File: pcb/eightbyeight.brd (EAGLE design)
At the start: 60 x 60 mm, 163 parts, among them J1 USB_MICROSMT+THRUHULE, J2 BATTERY, Q1 16MHz, SW1 SWITCH_SPDT, SW2 BRIGHTNESS, U1 MK20DN64VFM5, U10 FDG6316P, U11 FDG6316P, U12 FDG6316P, U2 ICN2026, U3 74138, U4 ICN2026, U5 MIC5219 3.3V, U6 ESP_WROOM_02, U7 MP3401A, U8 MMA8653FC, U9 FDG6316P

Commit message: Add HRC art
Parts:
- R28: value DNP -> 10k
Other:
- outline, holes or cut-outs redrawn
- board text added: "EightByEight RevF 2016-07"
- board text added: "Silk layers: 200: 2 sigma front (LED side) 201: 2 sigma back (component side) 203: HRC front (LED side) 204: Blinkinlabs front (LED side)"
- board text removed: "EightByEight RevE 2016-07"

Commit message: Production silk and component values
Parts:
- R1: value 1.6k 1% -> 1k 1%
- R9: value 2k 1% -> 1k 1%
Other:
- board text added: "Silk layers: 200: 2 sigma bottom (LED side) 201: 2 sigma top (component side) 203: HRC back (LED side) 204: Labels top (component side) 206: Blinkinlabs top (component side)"
- board text removed: "16"
- board text removed: "3.3V"
- board text removed: "5"
- board text removed: "Blinkinlabs, LLC"
- board text removed: "Charge"
- board text removed: "EightByEight RevF 2016-07"
- board text removed: "GND"
- board text removed: "Off"
- board text removed: "On"
- board text removed: "Power"
- board text removed: "Silk layers: 200: 2 sigma front (LED side) 201: 2 sigma back (component side) 203: HRC front (LED side) 204: Blinkinlabs front (LED side)"

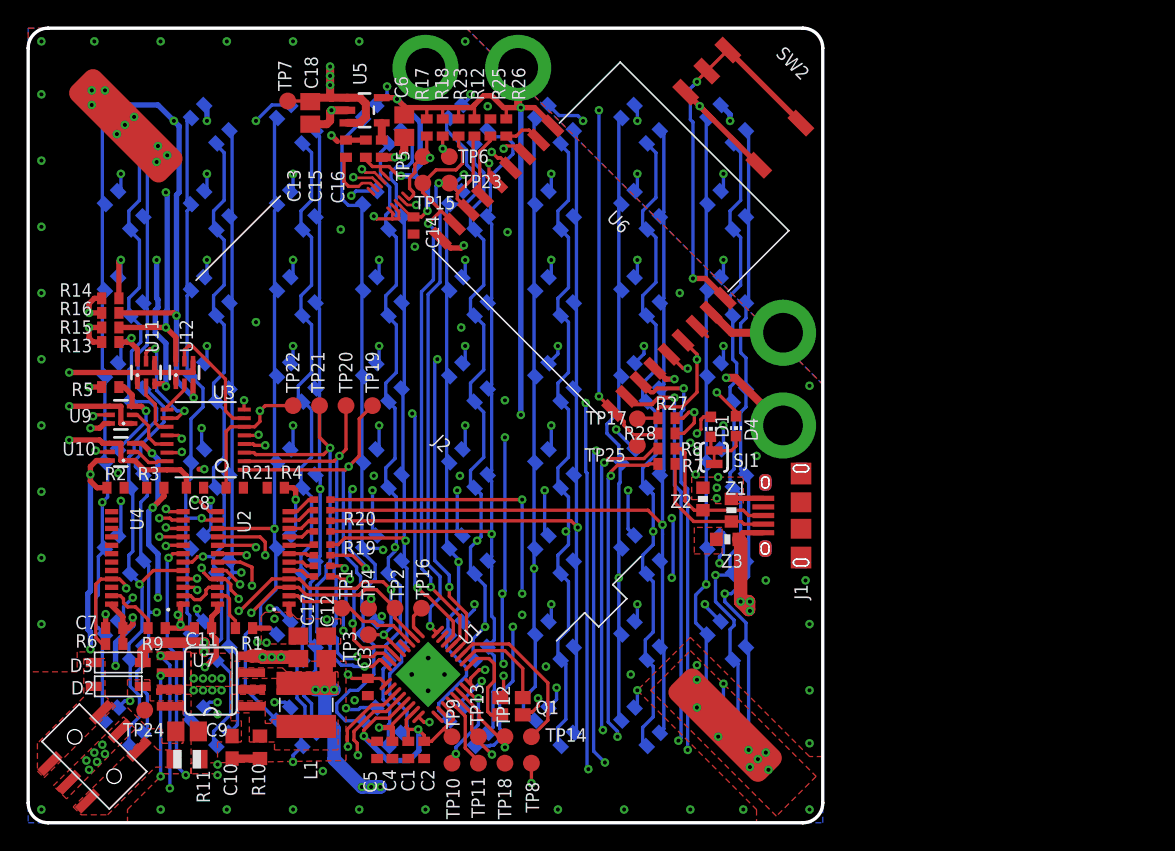
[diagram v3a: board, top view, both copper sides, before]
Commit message: Add battery protection circuit
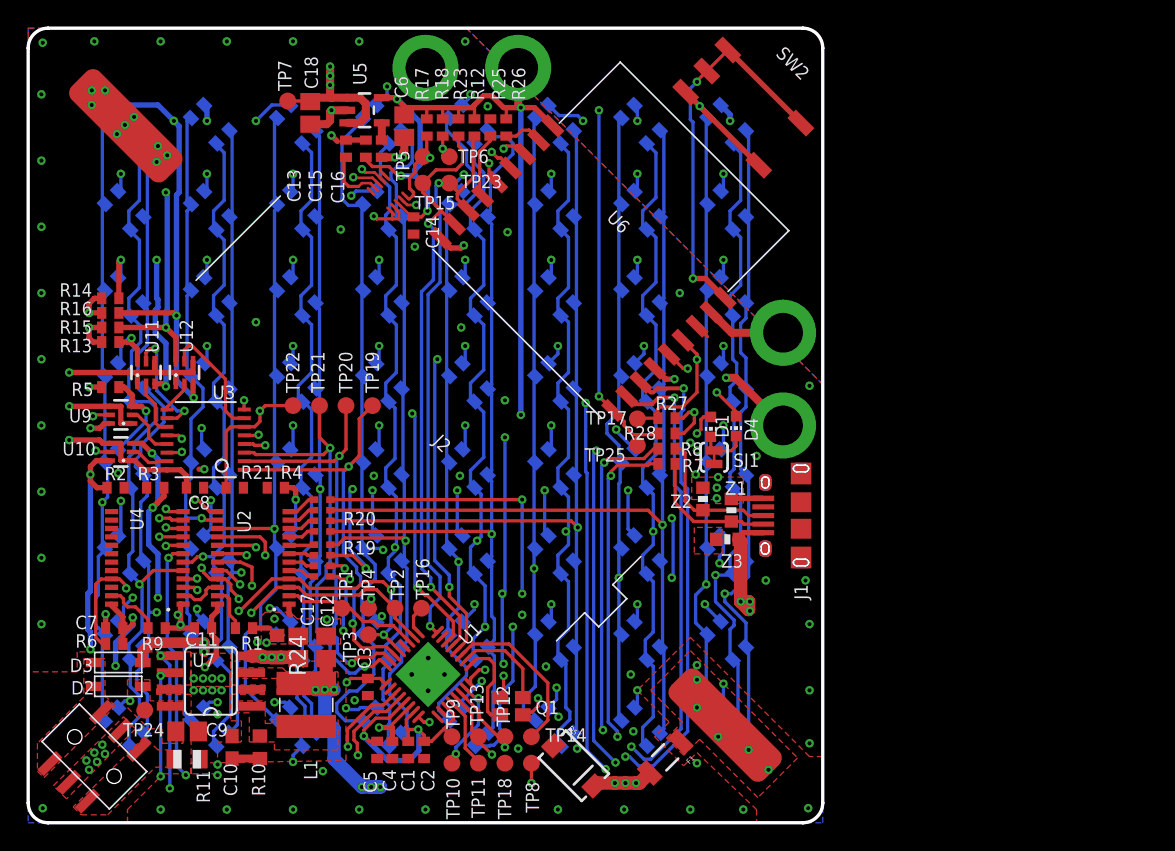
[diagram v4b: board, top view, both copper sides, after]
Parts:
- added D5: 1N5822, SparkFun-DiscreteSemi:SMA-DIODE
- added F1: PTCSMD-W, SparkFun-PowerIC:PTC-1206-WIDE
- added R24: 510, adafruit:R0603
- D2, D3: value RB161M-20 -> 1N5819
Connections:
- new net VBAT_FUSED: C12.1, D5.C, F1.2, L1.P$1, TP8.TP, U7.3
- net GND: now also D5.A, R24.1
- net USB_5V: now also R24.2
- net VBAT: now also F1.1; no longer C12.1, L1.P$1, TP8.TP, U7.3
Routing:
- net VBAT: track 46.6 -> 0.00 mm, vias 16 -> 6
- net VBAT_FUSED: track 0.00 -> 40.5 mm, vias 0 -> 10
- net DISCHARGE: track 84.0 -> 85.8 mm
- net CHARGE: track 77.2 -> 78.3 mm
- net ARM_TX: track 49.4 -> 50.1 mm
- net GND: vias 102 -> 107
- added copper zone on layer 1, net VBAT_FUSED

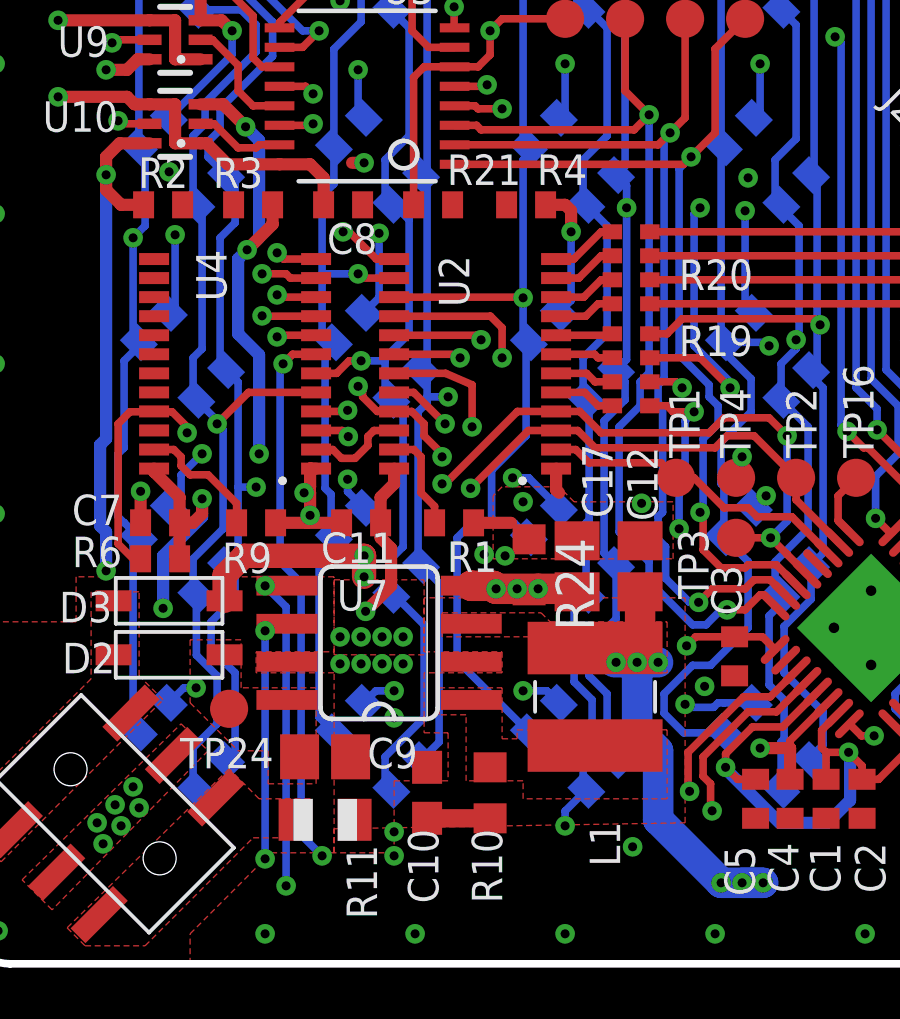
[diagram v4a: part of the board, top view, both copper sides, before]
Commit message: Add seperate bleed resistor to 5V input
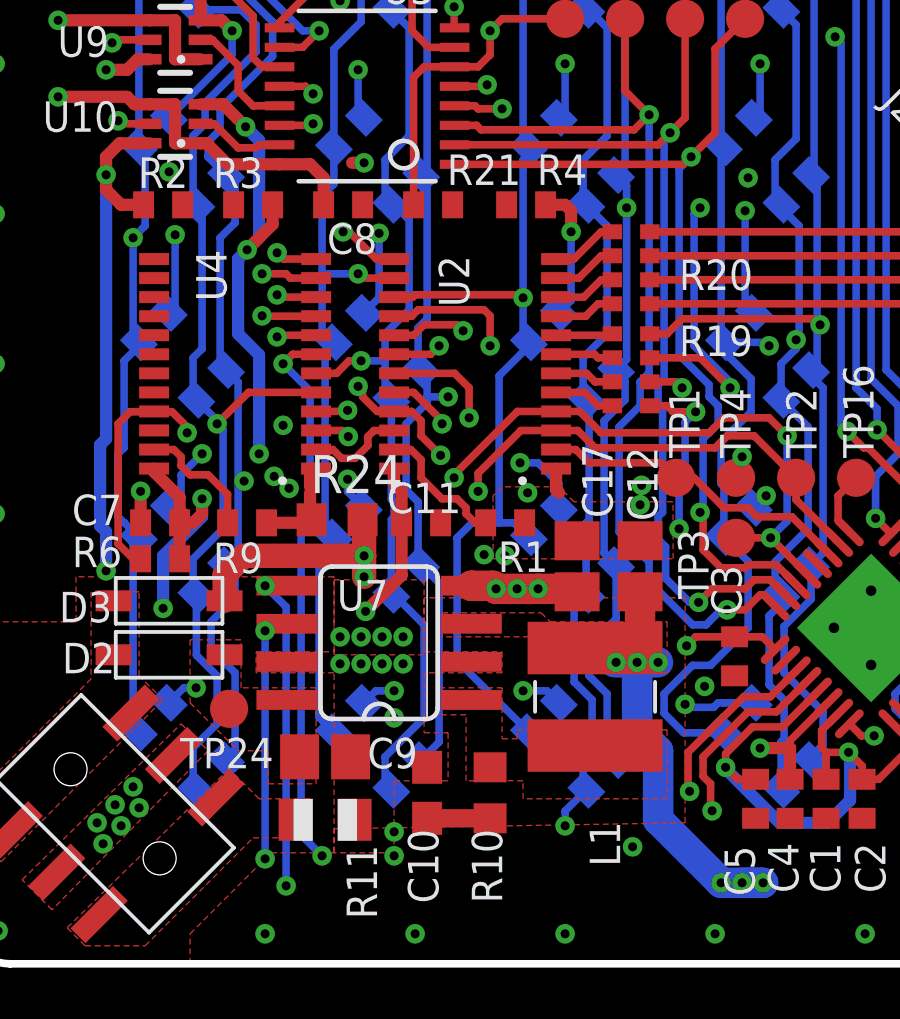
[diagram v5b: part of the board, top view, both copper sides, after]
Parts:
- moved R24 6.57 mm to (12.4, 14.8), turned to 0 degrees
- moved C11 2.00 mm to (15.2, 14.7), turned to 0 degrees
- moved R1 1.70 mm to (18.0, 14.7)
- moved R9 0.30 mm to (9.40, 14.7)
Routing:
- net GND: track 73.3 -> 70.7 mm, vias 107 -> 109
- net 1ROW1: track 73.1 -> 74.3 mm
- net USB_5V: track 65.4 -> 66.7 mm
- net N$18: track 3.39 -> 4.53 mm

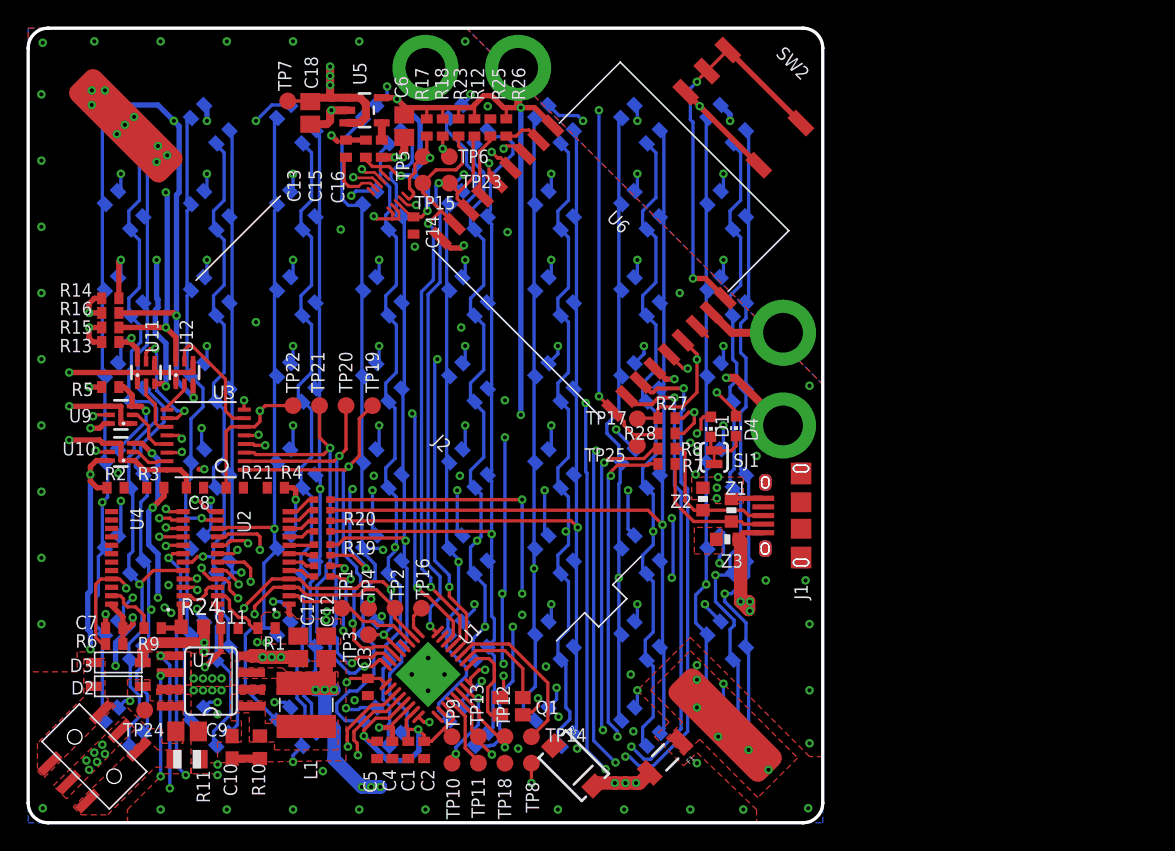
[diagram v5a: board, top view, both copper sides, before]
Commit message: Replace 0402 components, add RevH notes
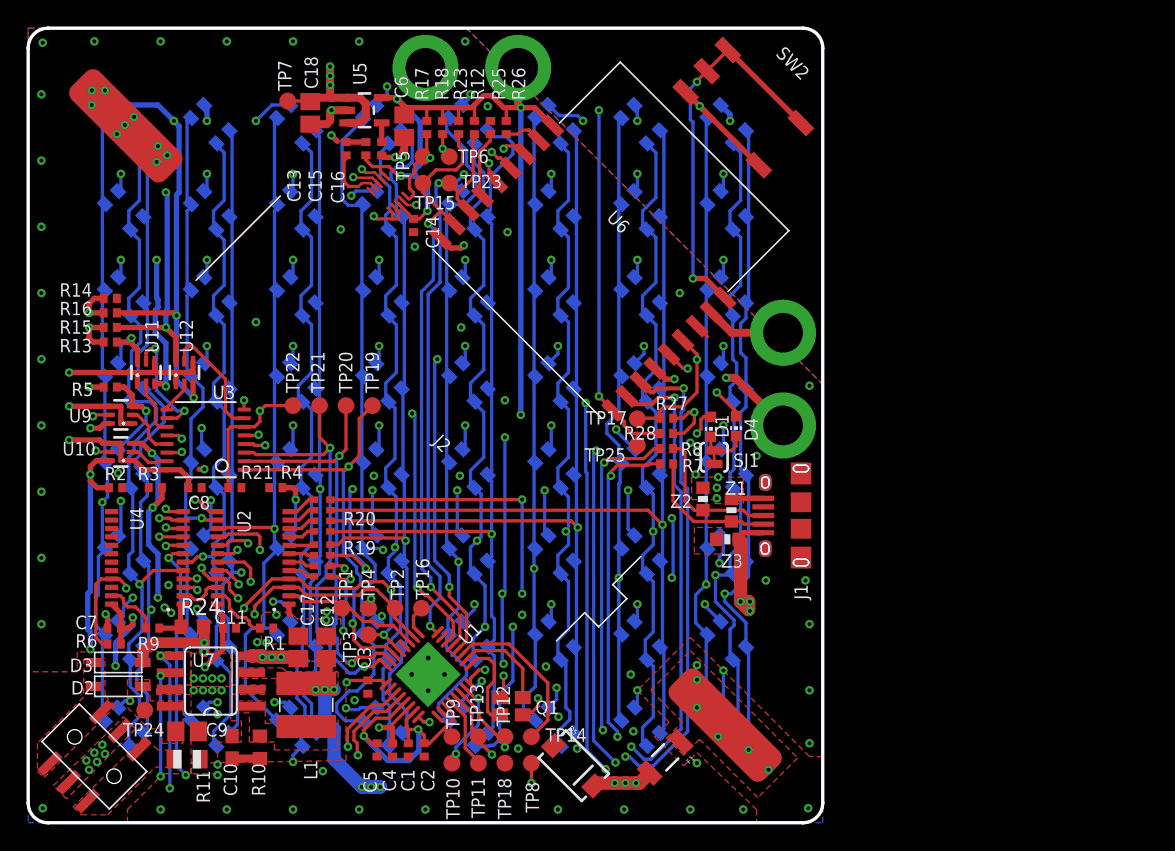
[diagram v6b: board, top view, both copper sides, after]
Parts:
- C1, C11, C13, C14, C15, C16, C2, C3, C4, C5, C7, C8: device adafruit:C0402 -> DevicesToMerge:CAP_0402
- J2: value BATTERY -> BATTERYAA_SMD
- LED_1, LED_10, LED_11, LED_12, LED_13, LED_14, LED_15, LED_16, LED_17, LED_18, LED_19, LED_2, LED_20, LED_21, LED_22, LED_23, LED_24, LED_25, LED_26, LED_27, LED_28, LED_29, LED_3, LED_30, LED_31, LED_32, LED_33, LED_34, LED_35, LED_36, LED_37, LED_38, LED_39, LED_4, LED_40, LED_41, LED_42, LED_43, LED_44, LED_45, LED_46, LED_47, LED_48, LED_49, LED_5, LED_50, LED_51, LED_52, LED_53, LED_54, LED_55, LED_56, LED_57, LED_58, LED_59, LED_6, LED_60, LED_61, LED_62, LED_63, LED_64, LED_7, LED_8, LED_9: value LED_RGB_CA -> LED_RGB_CA3528
- R1, R12, R13, R14, R15, R16, R17, R18, R2, R21, R23, R25, R26, R27, R28, R3, R4, R5, R6, R7, R8, R9: device adafruit:R0402 -> DevicesToMerge:RESISTOR_0402
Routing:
- net 1ROW5: track 70.5 -> 67.5 mm
- net 1ROW0: track 85.7 -> 87.2 mm
- net +3V3: track 81.2 -> 82.5 mm
- net ARM_3V3: track 64.0 -> 65.0 mm
- net GND: track 70.7 -> 71.4 mm
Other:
- board text added: "EightByEight Blinky 2017-02-11 RevH"

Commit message: Use copper fills for 5v, battery traces
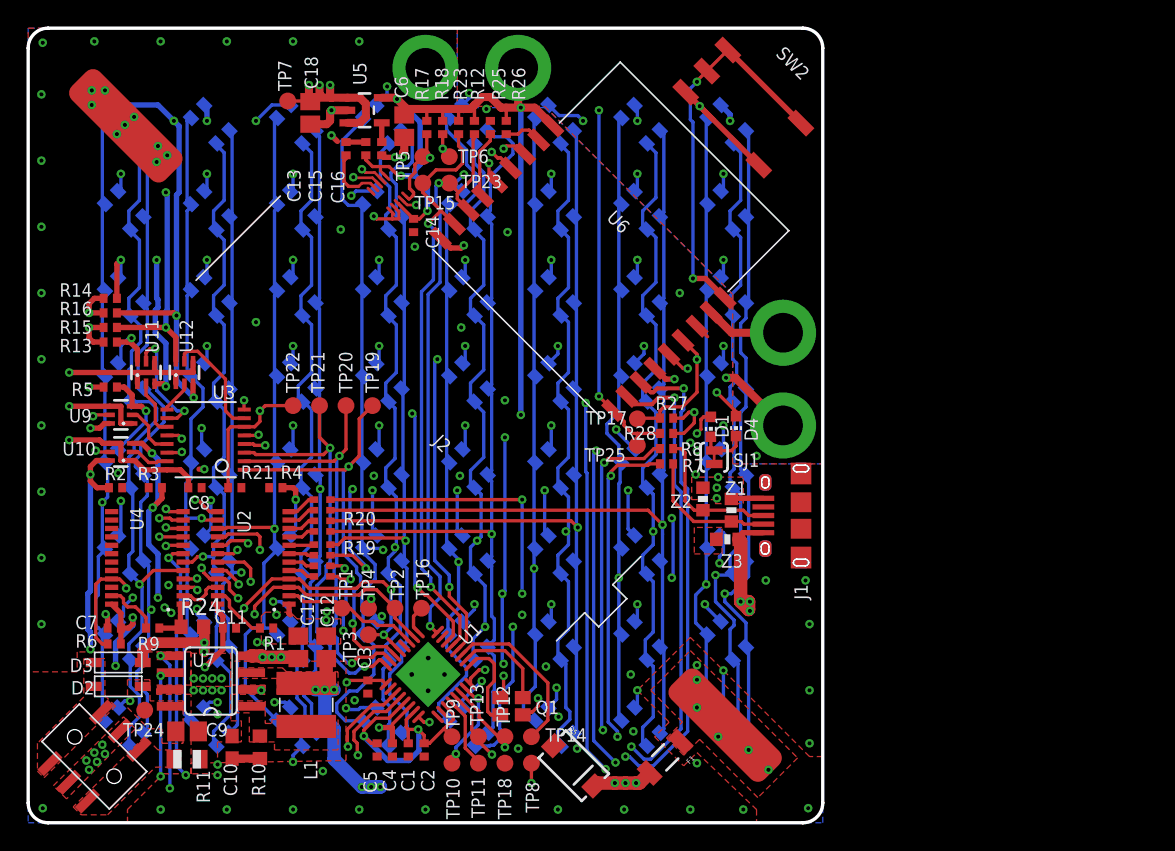
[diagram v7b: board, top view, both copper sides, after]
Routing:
- net +5V: track 140.6 -> 47.2 mm
- net USB_5V: track 66.7 -> 21.2 mm
- net VBAT_FUSED: track 40.5 -> 19.7 mm
- net 1ROW5: track 67.5 -> 70.6 mm
- net LED_S7: track 9.16 -> 8.65 mm
- net GND: vias 109 -> 108
- added copper zone on layer 15, net USB_5V
- added copper zone on layer 15, net VBAT_FUSED
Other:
- board text added: "+"
- board text added: "-"
- board text added: "EightByEight Blinky 2017-02-12 RevH"
- board text removed: "EightByEight Blinky 2017-02-11 RevH"

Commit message: Replace caps and resistors
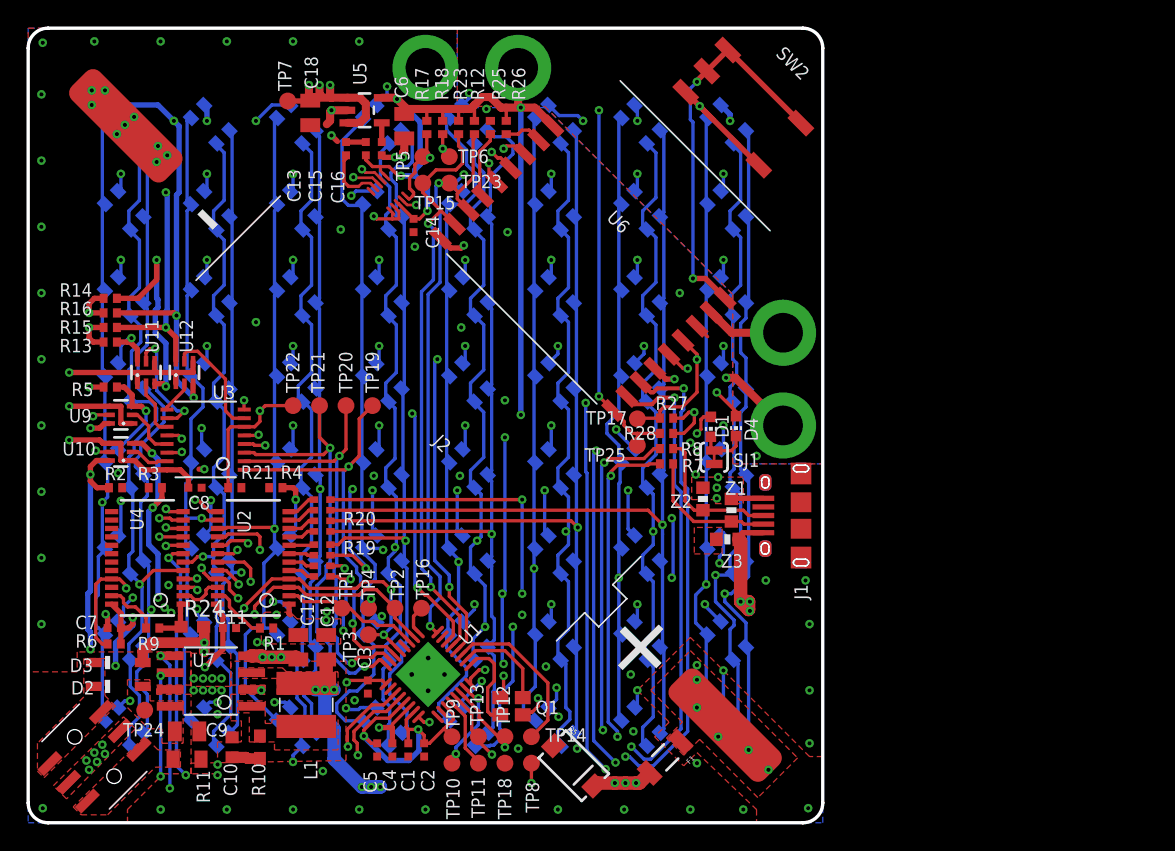
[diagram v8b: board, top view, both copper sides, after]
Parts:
- C1, C11, C13, C14, C15, C16, C2, C3, C4, C5, C7, C8: device DevicesToMerge:CAP_0402 -> blinkinlabs:CAP_0402
- C10: device adafruit:C0603 -> blinkinlabs:CAP_0603
- C12, C17, C18, C6, C9: device adafruit:C0805 -> blinkinlabs:CAP_0805
- D2, D3: device adafruit:SOD-123 -> blinkinlabs:SOD-123
- R1, R12, R13, R14, R15, R16, R17, R18, R2, R21, R23, R25, R26, R27, R28, R3, R4, R5, R6, R7, R8, R9: device DevicesToMerge:RESISTOR_0402 -> blinkinlabs:R_0402
- R10, R24: device adafruit:R0603 -> blinkinlabs:R_0603
- R11: device adafruit:R0805 -> blinkinlabs:R_0805
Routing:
- net 1ROW5: track 70.6 -> 72.6 mm
- net GND: track 71.4 -> 70.1 mm
